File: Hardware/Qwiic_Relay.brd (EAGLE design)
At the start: 25.4 x 50.8 mm, 34 parts, among them J2 Qwiic Right Angle, J3 Qwiic Right Angle, J4 AVR_SPI_PROG_3X2TESTPOINTS, Q4 600mA/40V, U1 ATTIN85_SOIC_5.3MM, U2 OPTO_ISOLATOR_DIP

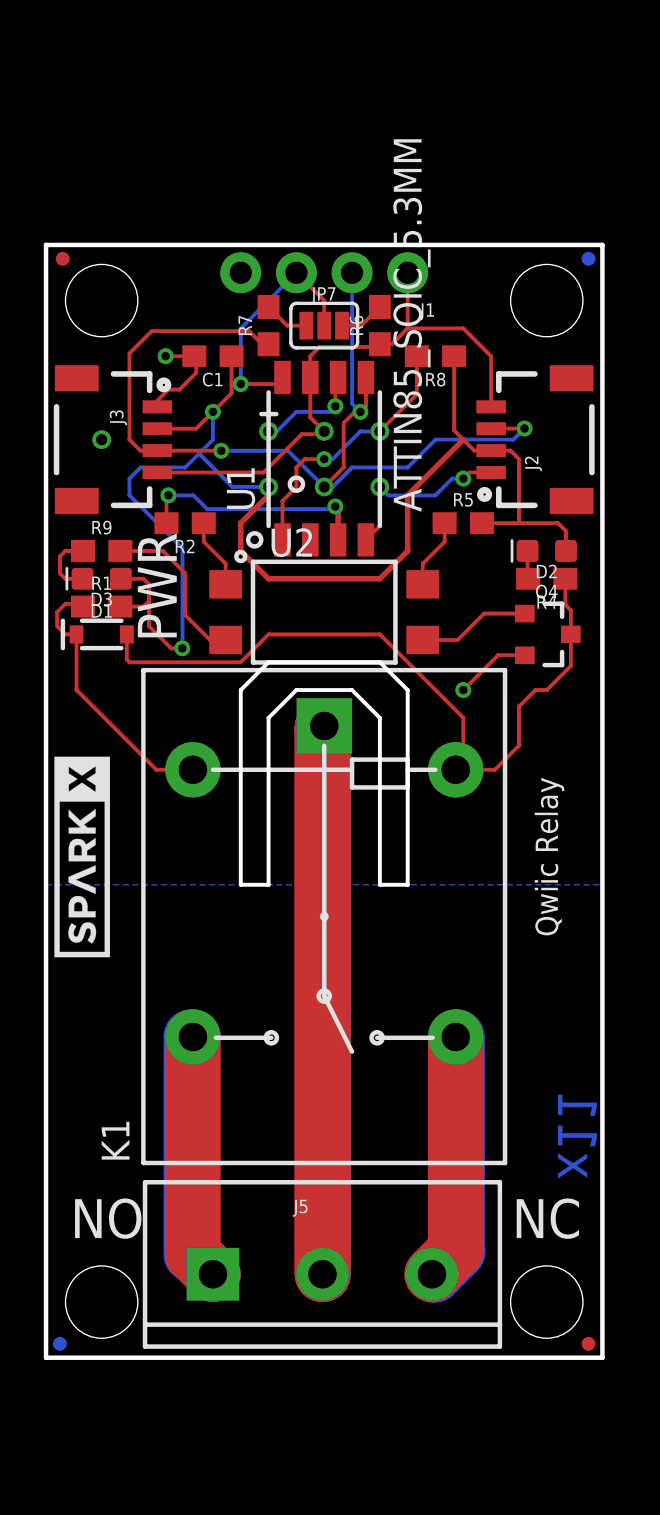
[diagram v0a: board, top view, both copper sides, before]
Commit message: moved the coil trace outside of the routeout
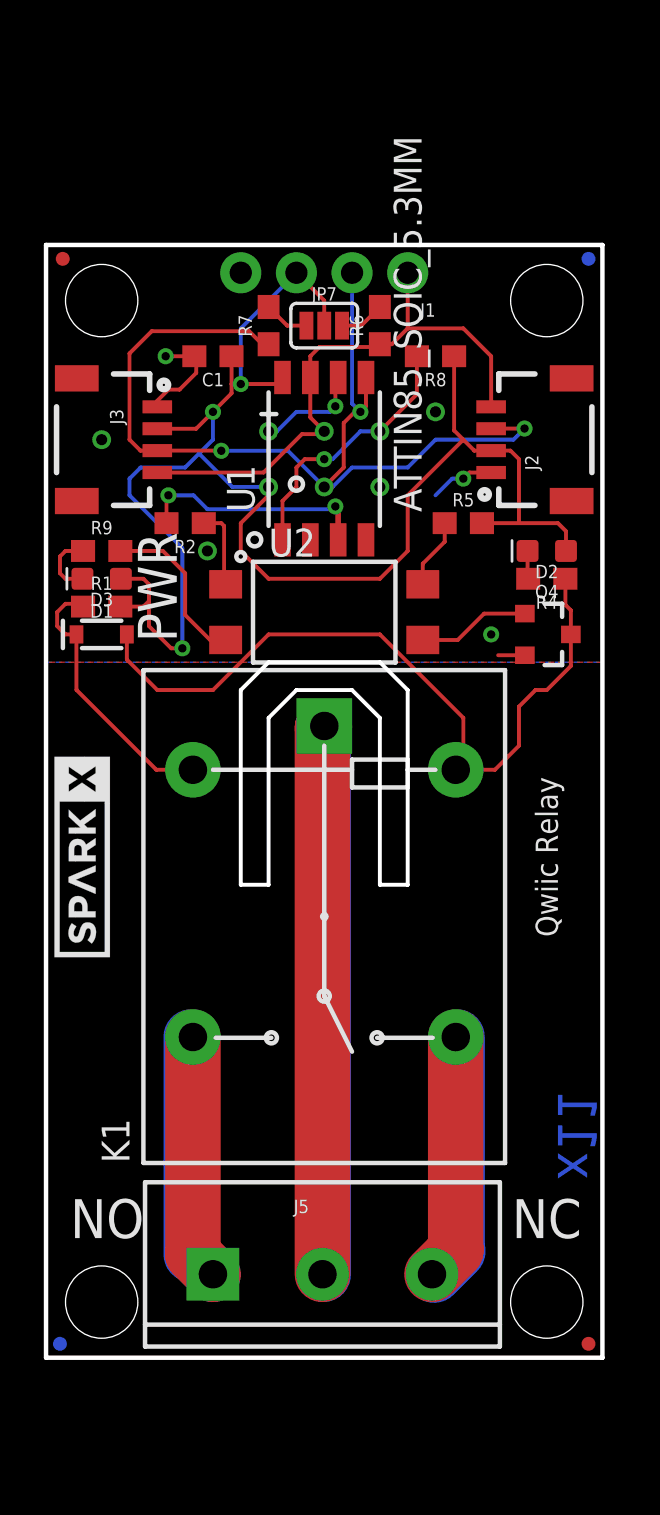
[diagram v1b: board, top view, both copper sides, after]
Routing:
- net COM: track 75.0 -> 50.0 mm
- net GND: track 24.1 -> 16.5 mm, vias 4 -> 6
- net N$2: track 34.6 -> 35.7 mm

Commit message: Rev 2 and sent to fab
Revision 2 of the board. (x12)

added more clearance to the PCB
added buzzard labels
added cutout into the dimension layer so that it is exported to GKO

fixed spacing on the Schematic
added address jumper to pin 2 of the ATtiny85

on the panel sent off to production
- labeled the cutout as "cutout" in the GKO
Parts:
- added JP10: JUMPER-SMT_2_NO_NO-SILK, SparkFun-Jumpers:SMT-JUMPER_2_NO_NO-SILK
- added U$10: (no value), buzzard_labels:ACT5
- added U$11, U$18: (no value), buzzard_labels:NO2
- added U$12: (no value), buzzard_labels (1):COM7
- added U$15, U$16: (no value), buzzard_labels:QWIIC_RELAY1
- added U$17, U$20: (no value), buzzard_labels:NC3
- added U$19: (no value), buzzard_labels:COM4
- added U$2: (no value), Labels-0_04:(PWR)
- added U$5: (no value), Labels-0_04:SCL
- added U$6: (no value), Labels-0_04:SDA
- added U$7: (no value), Labels-0_04:3.3V
- added U$8: (no value), Labels-0_04:GND
- added U$9: (no value), Labels-0_04:(ADR)
- K1: device Relay_SPDT:RELAY_SPDT_1C -> SparkX:RELAY_SPDT_1C
- U2: value OPTO_ISOLATOR_DIP -> OPTO_ISOLATOR; device LTV-816:4PIN_DIP -> SparkX:4PIN_DIP
- moved J5 10.2 mm to (17.8, 5.08), turned to 180 degrees
- moved JP1 5.08 mm to (2.54, -2.54)
- moved JP5 5.08 mm to (22.9, -2.54)
- moved U$3 2.59 mm to (2.16, 20.3)
- moved U$4 2.59 mm to (2.16, 20.3), turned to 270 degrees
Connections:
- new net N$5: JP10.1, U1.2
- net GND: now also JP10.2
- net NC: now also J5.1; no longer J5.3
- net NO: now also J5.3; no longer J5.1
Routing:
- net COM: track 50.0 -> 71.3 mm
- net NC: track 22.6 -> 38.1 mm
- net N$5: track 0.00 -> 15.6 mm, vias 0 -> 1
- net NO: track 22.4 -> 20.0 mm
- net N$2: track 35.7 -> 33.8 mm, vias 0 -> 1
- net N$13: track 3.06 -> 1.28 mm
- net N$7: track 12.4 -> 10.9 mm
- net 3.3V: track 75.2 -> 74.1 mm
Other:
- board size 25.4 x 50.8 mm -> 25.4 x 55.9 mm
- board text added: "Max Current 5.5A @ 240VAC 100 mil width 15 *C Rise 1 Oz Cu"
- board text added: "x12"
- board text removed: "3.3V"
- board text removed: "COM"
- board text removed: "GND"
- board text removed: "Max Current 5.5A 100 mil width 15 *C Rise 1 Oz Cu"
- board text removed: "NC"
- board text removed: "NO"
- board text removed: "PWR"
- board text removed: "Qwiic Relay"
- board text removed: "SCL"
- board text removed: "SDA"
- board text removed: "x11"
